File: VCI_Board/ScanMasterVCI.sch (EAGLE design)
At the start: 77 parts, among them IC1 XMEGA16A4A, Q13 MMBT3904, Q14 MMBT3904, Q15 MMBT3904, Q2 NDC7002N, Q3 MMBT3904, Q5 NTZD5110N, Q6 MMBT3904, Q7 ZXMP6A17G, Q8 MMBT4403, Q9 NDC7002N, U1 MAX17502FATB+, U2 SN65HVDA195-Q1, U3 MAX17502EATB+, U4 L78L08ABUTR

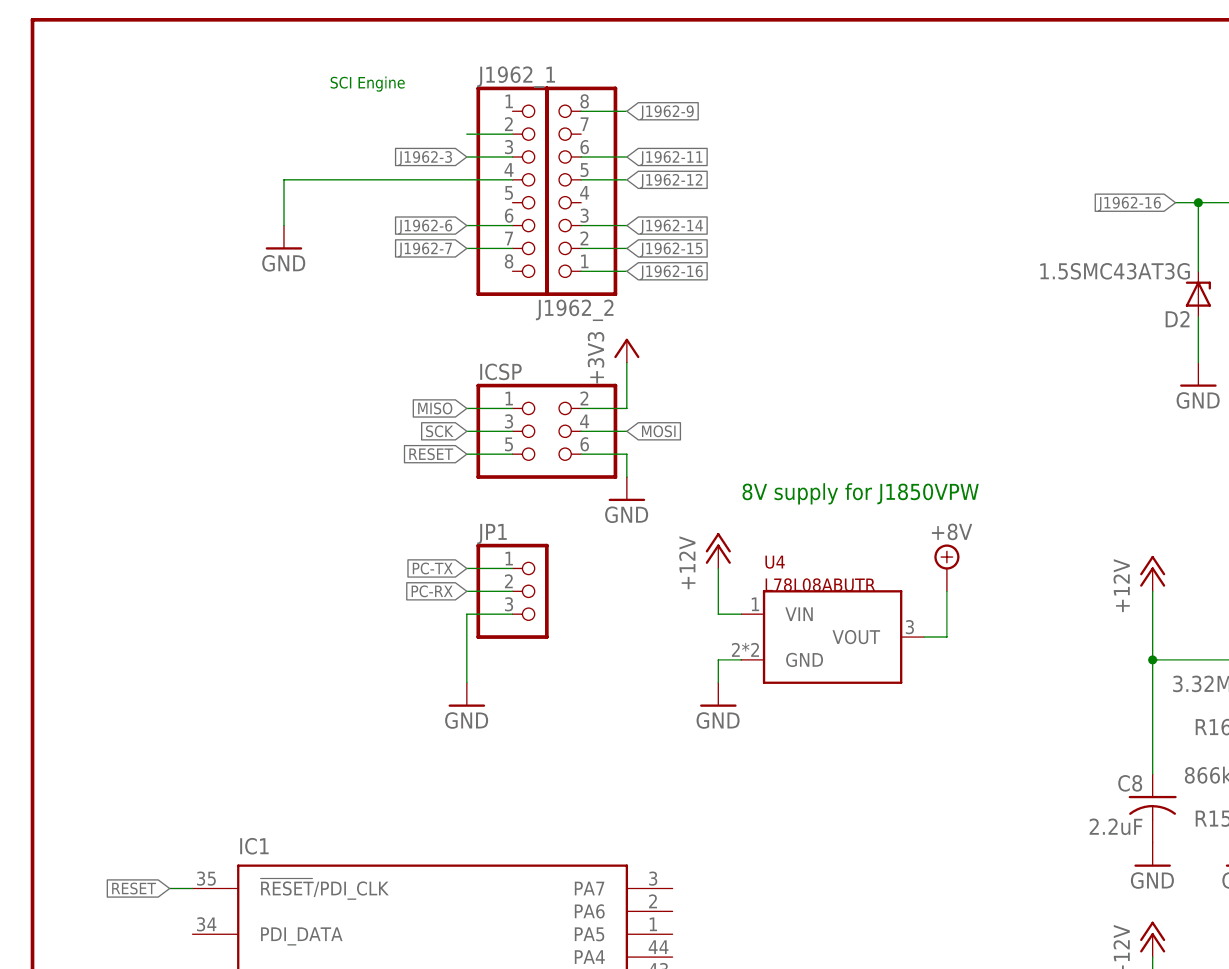
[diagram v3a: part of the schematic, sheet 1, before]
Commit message: Changed OBD2 connector, refined layout
Decided that it'd be more efficient if I removed all un-used OBD-II pins. Axed about 5 pins and changed the order such that the layout is easier. Managed to get the number of vias down to 68 or so. Separated resistors and capacitors into rows so that I can label them individually.
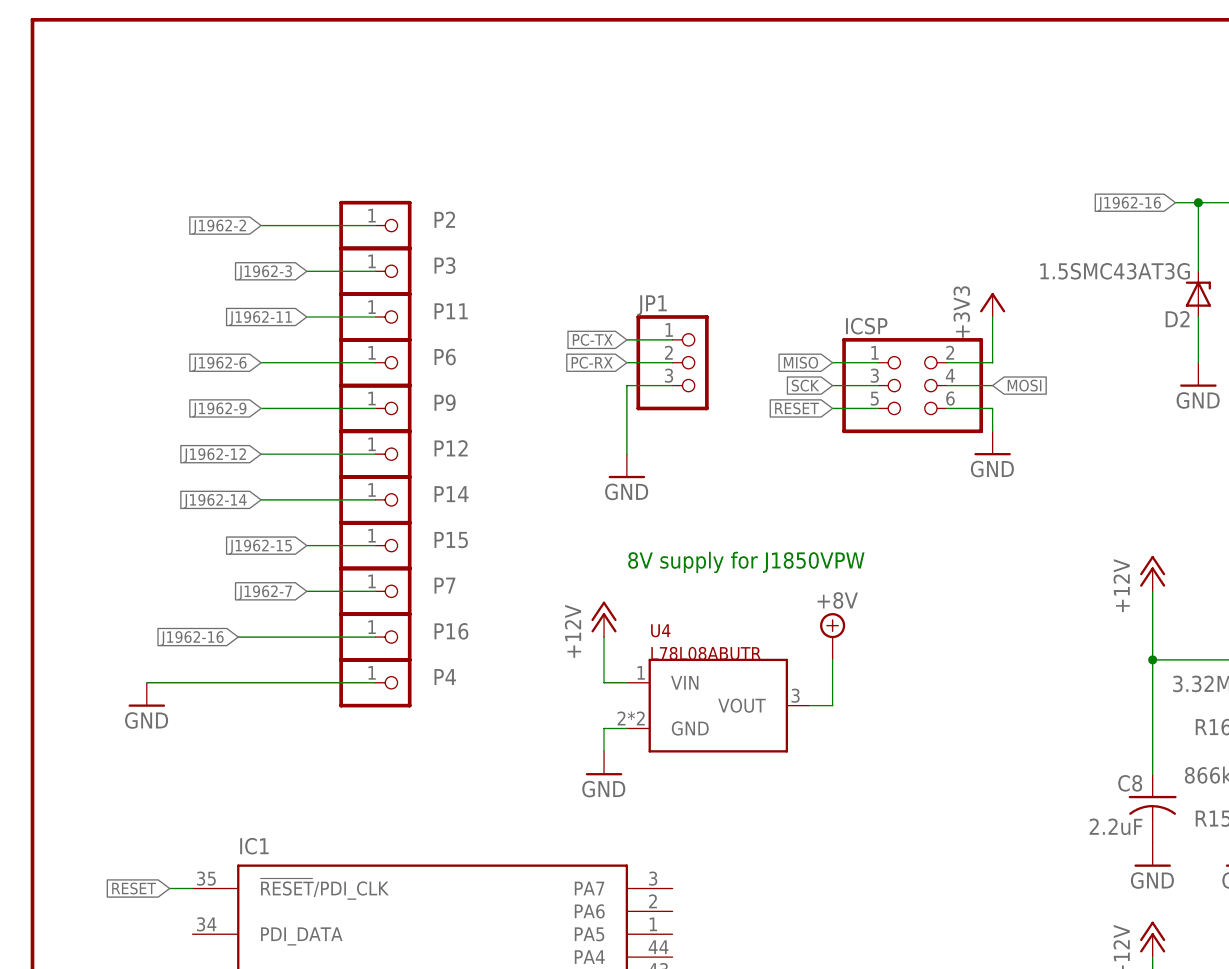
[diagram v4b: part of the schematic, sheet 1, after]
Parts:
- removed J1962_1, J1962_2: (no value), pinhead:PINHD-1X8
- added P11, P12, P14, P15, P16, P2, P3, P4, P6, P7, P9: (no value), pinhead:PINHD-1X1
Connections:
- net GND: now also P4.1; no longer J1962_1.4
- net J1962-11: now also P11.1; no longer J1962_2.6
- net J1962-12: now also P12.1; no longer J1962_2.5
- net J1962-14: now also P14.1; no longer J1962_2.3
- net J1962-15: now also P15.1; no longer J1962_2.2
- net J1962-16: now also P16.1; no longer J1962_2.1
- net J1962-2: now also P2.1; no longer J1962_1.2
- net J1962-3: now also P3.1; no longer J1962_1.3
- net J1962-6: now also P6.1; no longer J1962_1.6
- net J1962-7: now also P7.1; no longer J1962_1.7
- net J1962-9: now also P9.1; no longer J1962_2.8
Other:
- note removed: "SCI Engine"
- moved on the sheet: ICSP, JP1, U4

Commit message: Replaced NDC7002N with NTZD5110N
NDC7002N is out of stock at Digikey, so I am substituting the NTZD5110N. Should be fine, the 5110 just has a lower amp rating than the 7002.
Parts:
- removed Q9: NDC7002N, customics:NDC7002N
- added Q1: NTZD5110N, customics:NTZD5110N
- Q2: value NDC7002N -> NTZD5110N; device customics:NDC7002N -> customics:NTZD5110N
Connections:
- net ISO-K: now also Q1B.D; no longer Q9B.D
- net J1962-11: now also R1.2, U$1.CANL; no longer R1.1, U$1.CANH
- net J1962-3: now also R1.1, U$1.CANH; no longer R1.2, U$1.CANL
- net J1962-7: now also Q1A.D; no longer Q9A.D
- net N$11: now also Q1A.G, Q1B.G; no longer Q9A.G, Q9B.G
- net N$4: now also Q1A.S, Q1B.S; no longer Q9A.S, Q9B.S

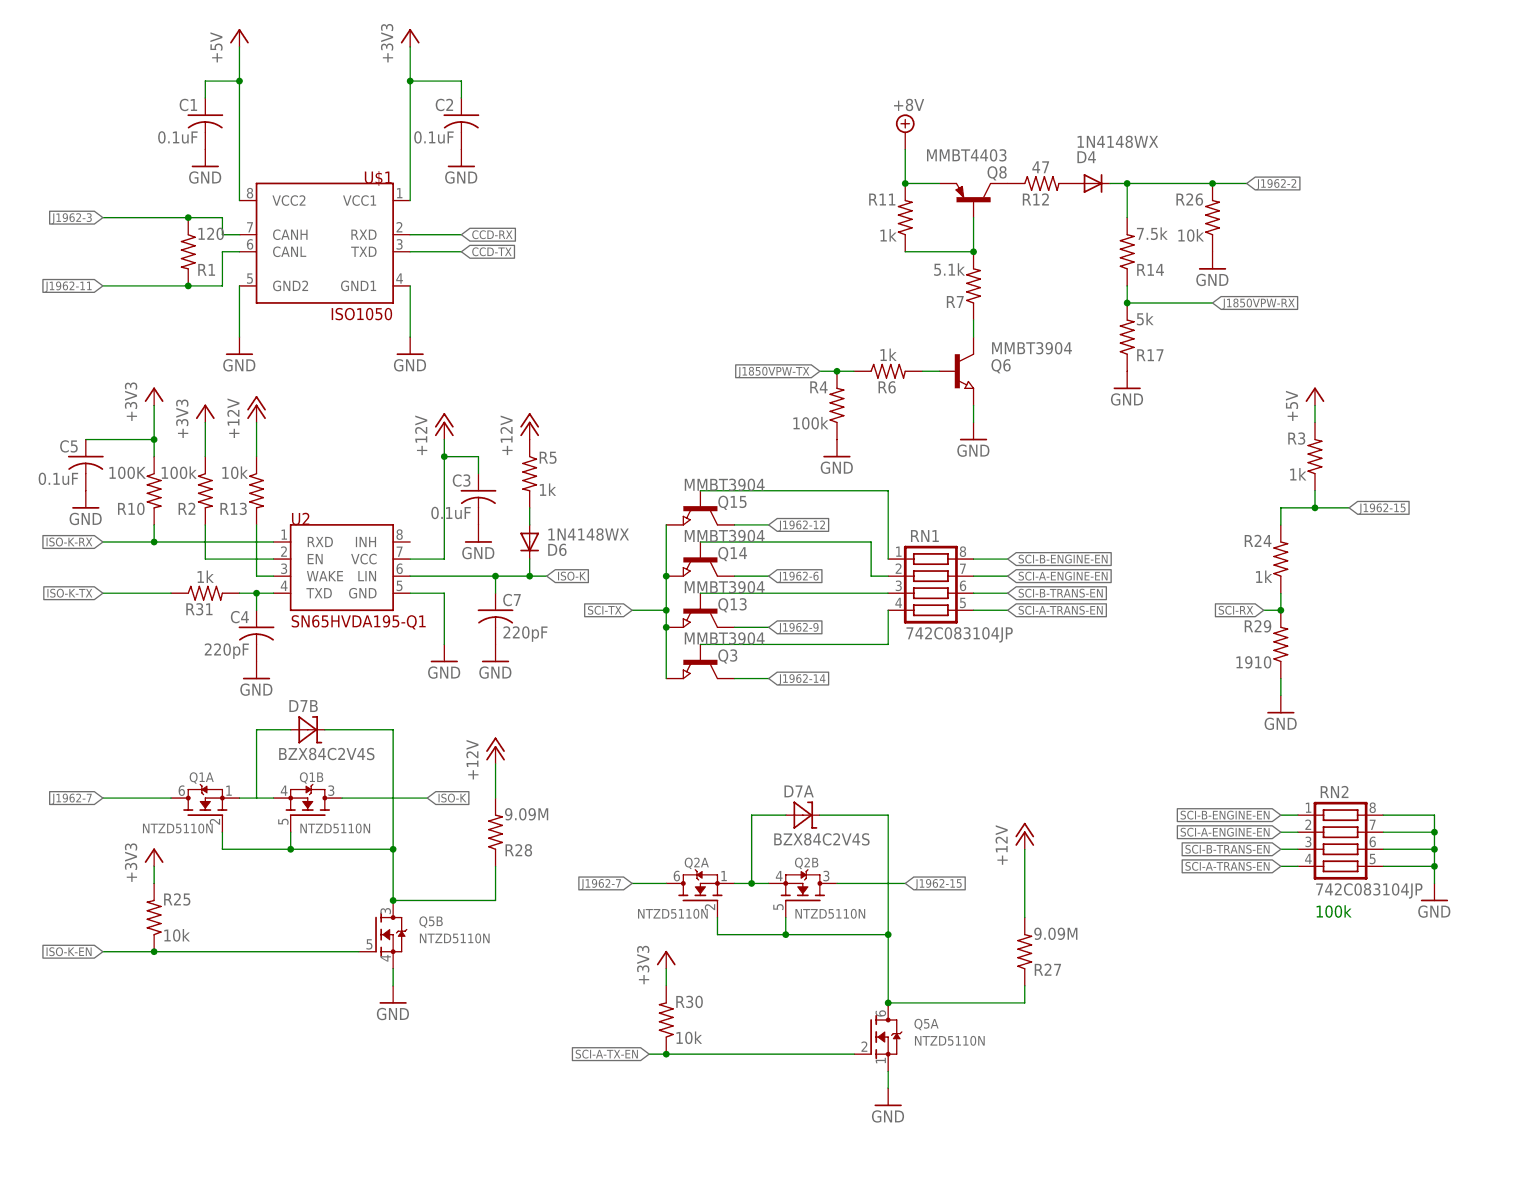
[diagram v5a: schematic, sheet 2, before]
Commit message: Re-positioned names, removed values
In layout, positioned names so they will be visible during assembly, and deleted values from layout, unneeded. Added another resistor array to save on space, number of vias down to 58.
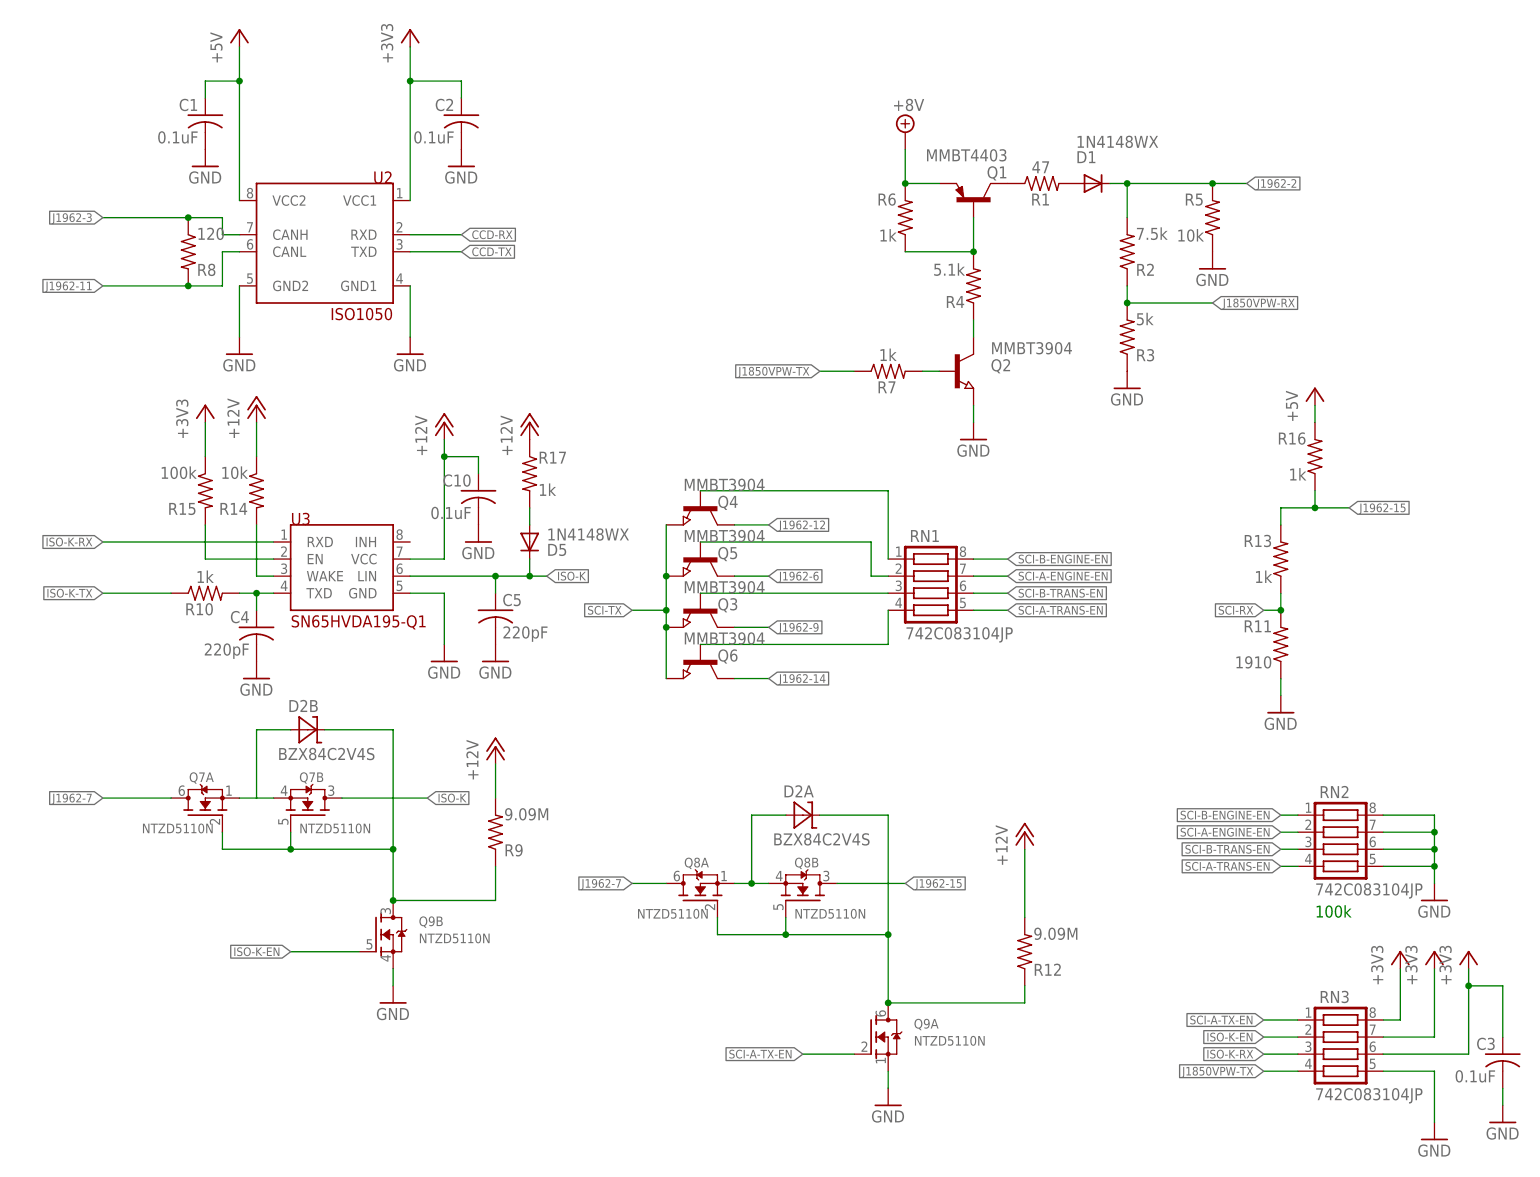
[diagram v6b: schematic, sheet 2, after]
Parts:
- removed C18: 100uF, adafruit:C-USC0603
- removed C19: 330pF, adafruit:C-USC0603
- removed FRAME1: FRAME-LETTER, SparkFun-Aesthetics:FRAME-LETTER
- removed P14, P15: (no value), pinhead:PINHD-1X1
- removed Q13, Q14: MMBT3904, semicon-smd-ipc:NPN-TRANSISTOR_SOT23
- removed R24, R31: 1k, adafruit:R-US_R0603
- removed R25, R26, R30: 10k, adafruit:R-US_R0603
- removed R27, R28: 9.09M, adafruit:R-US_R0603
- removed R29: 1910, adafruit:R-US_R0603
- removed U$1: ISO1050, customics:ISO1050
- added C16: 2.2uF, adafruit:C-USC0603
- added C6: 22uF, adafruit:C-USC0603
- added P1, P8: (no value), pinhead:PINHD-1X1
- added Q10: ZXMP6A17G, customics:ZXMP6A17G
- added Q9: NTZD5110N, customics:NTZD5110N
- added R18: 200k, adafruit:R-US_R0603
- added R19, R20: 866k, adafruit:R-US_R0603
- added R21: 20k, adafruit:R-US_R0603
- added RN3: 742C083104JP, resistor-net:CTS742C083
- added U5: MAX17502FATB+, customics:MAX17502
- C10, C13: value 1uF -> 0.1uF
- C11: value 2.2uF -> 1uF
- C12: value 22uF -> 1uF
- C14: value 3300pF -> 330pF
- C15: value 22uF -> 2.2uF
- C17: value 0.1uF -> 100uF
- C5: value 0.1uF -> 220pF
- C7: value 220pF -> 22uF
- C8: value 2.2uF -> 3300pF
- D1: value SMAJ5.0A -> 1N4148WX; device diode:ZENER-DIODESMB -> diode:DIODE-SOD323-R
- D2: value 1.5SMC43AT3G -> BZX84C2V4S; device diode:ZENER-DIODESMB -> customics:BZX84C2V4S
- D3: value MM5Z10V -> SMLVT3V3; device diode:DIODE-SOD523 -> diode:ZENER-DIODESMB
- D4: value 1N4148WX -> SMAJ5.0A; device diode:DIODE-SOD323-R -> diode:ZENER-DIODESMB
- D5: value SMLVT3V3 -> 1N4148WX; device diode:ZENER-DIODESMB -> diode:DIODE-SOD323-R
- D6: value 1N4148WX -> 1.5SMC43AT3G; device diode:DIODE-SOD323-R -> diode:ZENER-DIODESMB
- D7: value BZX84C2V4S -> MM5Z10V; device customics:BZX84C2V4S -> diode:DIODE-SOD523
- Q1: value NTZD5110N -> MMBT4403; device customics:NTZD5110N -> transistor-pnp:MMBT4403LT1SMD
- Q2, Q5: value NTZD5110N -> MMBT3904; device customics:NTZD5110N -> semicon-smd-ipc:NPN-TRANSISTOR_SOT23
- Q7: value ZXMP6A17G -> NTZD5110N; device customics:ZXMP6A17G -> customics:NTZD5110N
- Q8: value MMBT4403 -> NTZD5110N; device transistor-pnp:MMBT4403LT1SMD -> customics:NTZD5110N
- R1: value 120 -> 47
- R10: value 100K -> 1k
- R11: value 1k -> 1910
- R12: value 47 -> 9.09M
- R13: value 10k -> 1k
- R14: value 7.5k -> 10k
- R15: value 866k -> 100k
- R16: value 3.32M -> 1k
- R17: value 5k -> 1k
- R2: value 100k -> 7.5k
- R22: value 200k -> 3.32M
- R23: value 20k -> 3.32M
- R3: value 1k -> 5k
- R4: value 100k -> 5.1k
- R5: value 1k -> 10k
- R7: value 5.1k -> 1k
- R8: value 866k -> 120
- R9: value 3.32M -> 9.09M
- U1: value MAX17502FATB+ -> L78L08ABUTR; device customics:MAX17502 -> customics:L78L
- U2: value SN65HVDA195-Q1 -> ISO1050; device customics:SN65HVDA195-Q1 -> customics:ISO1050
- U3: value MAX17502EATB+ -> SN65HVDA195-Q1; device customics:MAX17502 -> customics:SN65HVDA195-Q1
- U4: value L78L08ABUTR -> MAX17502EATB+; device customics:L78L -> customics:MAX17502
- renumbered JP1 to SERIAL, P12 to P5, P16 to P10, Q15 to Q4
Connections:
- net +12V: now also C10.1, C14.1, C15.1, C16.1, C17.1, R12.2, R14.1, R17.1, R22.2, R23.2, U3.VCC, U5.VIN; no longer C11.1, C18.1, C19.1, C3.1, C8.1, R13.1, R16.2, R27.2, R28.2, R5.1, U2.VCC, U3.VIN
- net +3V3: now also C3.1, C6.1, D3.C, R15.1, RN3.6, RN3.7, RN3.8, U2.VCC1, U4.FB_VO; no longer C12.1, C5.1, D5.C, R10.1, R2.1, R25.2, R30.2, U$1.VCC1, U3.FB_VO
- net +5V: now also C7.1, D4.C, R16.2, U2.VCC2, U5.FB_VO; no longer C15.1, D1.C, R3.2, U$1.VCC2, U1.FB_VO
- net +8V: now also Q1.E, R6.2, U1.VOUT; no longer Q8.E, R11.2, U4.VOUT
- net CCD-RX: now also U2.RXD; no longer U$1.RXD
- net CCD-TX: now also U2.TXD; no longer U$1.TXD
- net GND: now also C16.2, C6.2, D3.A, D4.A, D6.A, P11.1, Q2.E, Q9A.S, Q9B.S, R11.1, R19.1, R20.1, R21.1, R3.1, R5.1, RN3.5, U2.GND1, U2.GND2, U4.PGND, U5.GND, U5.PGND; no longer C18.2, C19.2, D1.A, D2.A, D5.A, P4.1, Q5A.S, Q5B.S, Q6.E, R15.1, R17.1, R23.1, R26.1, R29.1, R4.1, R8.1, U$1.GND1, U$1.GND2, U1.PGND, U2.GND, U3.PGND
- net ISO-K: now also C5.1, D5.C, Q7B.D, U3.LIN; no longer C7.1, D6.C, Q1B.D, U2.LIN
- net ISO-K-EN: now also Q9B.G, RN3.2; no longer Q5B.G, R25.1
- net ISO-K-RX: now also RN3.3, U3.RXD; no longer R10.2, U2.RXD
- net ISO-K-TX: now also R10.1; no longer R31.1
- net J1850VPW-RX: now also R2.1, R3.2; no longer R14.1, R17.2
- net J1850VPW-TX: now also R7.1, RN3.4; no longer R4.2, R6.1
- net J1962-11: now also P2.1, R8.2, U2.CANL; no longer P11.1, R1.2, U$1.CANL
- net J1962-14: now also P7.1, Q6.C; no longer P14.1, Q3.C
- net J1962-15: now also P9.1, Q8B.D, R13.2, R16.1; no longer P15.1, Q2B.D, R24.2, R3.1
- net J1962-16: now also D6.C, D7.C, Q10.S, R18.2; no longer D2.C, D3.C, Q7.S, R22.2
- net J1962-2: now also D1.C, P1.1, R2.2, R5.2; no longer D4.C, P2.1, R14.2, R26.2
- net J1962-3: now also R8.1, U2.CANH; no longer R1.1, U$1.CANH
- net J1962-6: now also Q5.C; no longer Q14.C
- net J1962-7: now also P8.1, Q7A.D, Q8A.D; no longer P7.1, Q1A.D, Q2A.D
- net J1962-9: now also P4.1, Q3.C; no longer P9.1, Q13.C
- net N$1: now also D2A.A, Q8A.S, Q8B.S; no longer D7A.A, Q2A.S, Q2B.S
- net N$10: now also R10.2, U3.TXD; no longer R31.2, U2.TXD
- net N$11: now also D2B.C, Q7A.G, Q7B.G, Q9B.D, R9.1; no longer D7B.C, Q1A.G, Q1B.G, Q5B.D, R28.1
- net N$12: now also U4.LX; no longer U3.LX
- net N$14: now also R14.2, U3.WAKE; no longer R13.2, U2.WAKE
- net N$15: now also C12.1, U5.VCC; no longer C13.1, U1.VCC
- net N$16: now also R20.2, R23.1, U5.EN_UVLO; no longer R15.2, R16.1, U1.EN_UVLO
- net N$17: now also C9.1, U5.SS; no longer C14.1, U1.SS
- net N$18: now also C13.1, Q10.D; no longer C17.1, Q7.D
- net N$19: now also U5.LX; no longer U1.LX
- net N$20: now also D7.A, Q10.G, R18.1, R21.2; no longer D3.A, Q7.G, R22.1, R23.2
- net N$21: now also Q5.B; no longer Q14.B
- net N$22: now also Q3.B; no longer Q13.B
- net N$23: now also Q6.B; no longer Q3.B
- net N$26: now also Q2.C, R4.1; no longer Q6.C, R7.1
- net N$28: now also Q1.B, R4.2, R6.1; no longer Q8.B, R11.1, R7.2
- net N$29: now also Q1.C, R1.1; no longer Q8.C, R12.1
- net N$3: now also C8.1, U4.SS; no longer C9.1, U3.SS
- net N$30: now also D1.A, R1.2; no longer D4.A, R12.2
- net N$31: now also D5.A, R17.2; no longer D6.A, R5.2
- net N$4: now also D2B.A, Q7A.S, Q7B.S; no longer D7B.A, Q1A.S, Q1B.S
- net N$5: now also D2A.C, Q8A.G, Q8B.G, Q9A.D, R12.1; no longer D7A.C, Q2A.G, Q2B.G, Q5A.D, R27.1
- net N$6: now also Q2.B, R7.2; no longer Q6.B, R6.2
- net N$7: now also R19.2, R22.1, U4.EN_UVLO; no longer R8.2, R9.1, U3.EN_UVLO
- net N$8: now also R15.2, U3.EN; no longer R2.2, U2.EN
- net N$9: now also C11.1, U4.VCC; no longer C10.1, U3.VCC
- net SCI-A-TX-EN: now also Q9A.G, RN3.1; no longer Q5A.G, R30.1
- net SCI-RX: now also R11.2, R13.1; no longer R24.1, R29.2
- net SCI-TX: now also Q5.E, Q6.E; no longer Q13.E, Q14.E
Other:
- moved on the sheet: C11, C12, C13, C14, C15, C17, C3, C5, C8, C9, P11, P2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
